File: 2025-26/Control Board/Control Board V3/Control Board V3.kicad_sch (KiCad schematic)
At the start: 0 parts

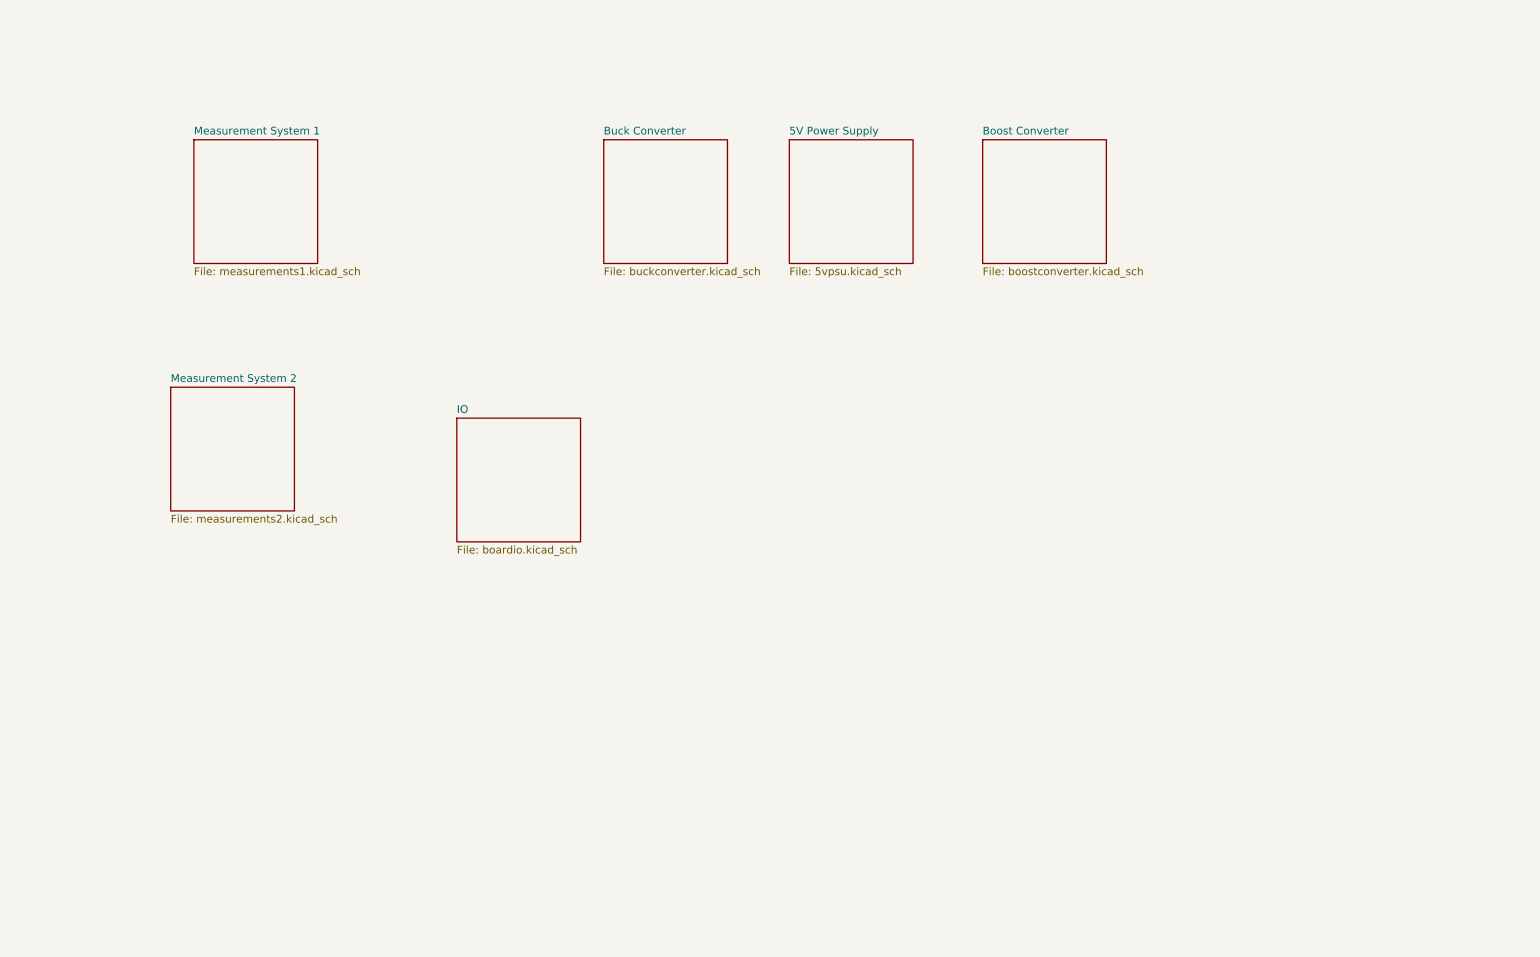
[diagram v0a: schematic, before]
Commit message: board almost fully designed
i want to try a different orientation so gonna push this so i can easily revert
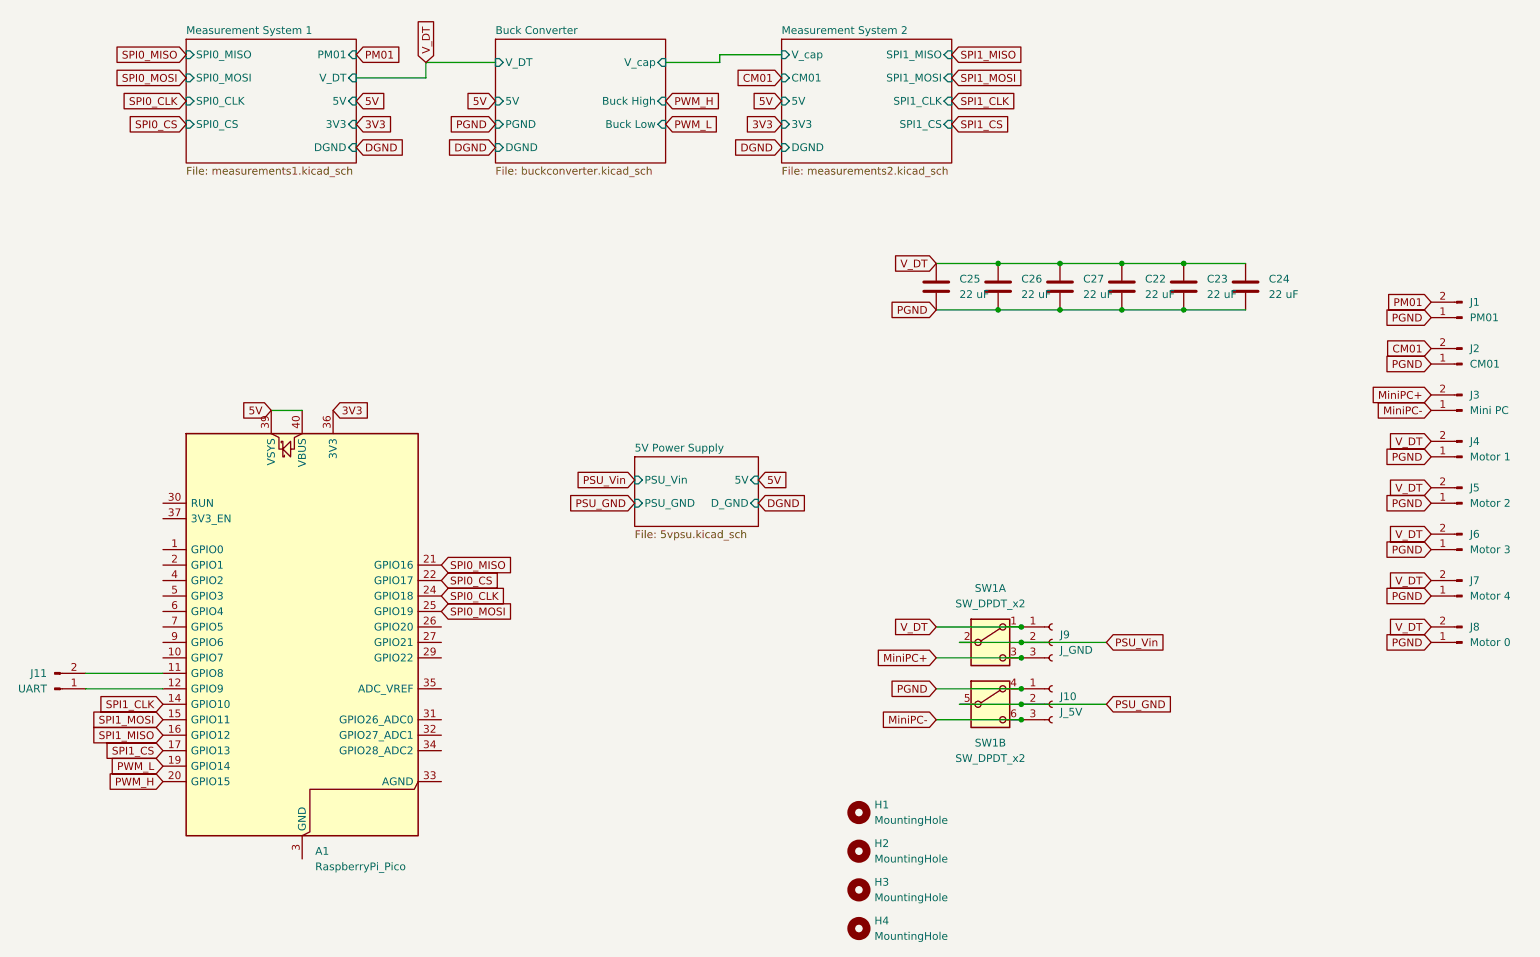
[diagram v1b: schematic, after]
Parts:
- added A1: RaspberryPi_Pico, Module:RaspberryPi_Pico_Common_Unspecified, symbol MCU_Module:RaspberryPi_Pico
- added C22, C23, C24, C25, C26, C27: 22 uF, Capacitor_SMD:C_0805_2012Metric, symbol Device:C
- added H1, H2, H3, H4: MountingHole, MountingHole:MountingHole_3.2mm_M3, symbol Mechanical:MountingHole
- added J1: PM01, Connector_AMASS:AMASS_XT30PW-F_1x02_P2.50mm_Horizontal, symbol Connector:Conn_01x02_Pin
- added J10: J_5V, Connector_PinHeader_2.54mm:PinHeader_1x03_P2.54mm_Vertical, symbol Connector:Conn_01x03_Socket
- added J11: UART, Connector_PinHeader_2.54mm:PinHeader_1x02_P2.54mm_Vertical, symbol Connector:Conn_01x02_Pin
- added J2: CM01, Connector_AMASS:AMASS_XT30PW-F_1x02_P2.50mm_Horizontal, symbol Connector:Conn_01x02_Pin
- added J3: Mini PC, Connector_AMASS:AMASS_XT30PW-F_1x02_P2.50mm_Horizontal, symbol Connector:Conn_01x02_Pin
- added J4: Motor 1, Connector_AMASS:AMASS_XT30PW-F_1x02_P2.50mm_Horizontal, symbol Connector:Conn_01x02_Pin
- added J5: Motor 2, Connector_AMASS:AMASS_XT30PW-F_1x02_P2.50mm_Horizontal, symbol Connector:Conn_01x02_Pin
- added J6: Motor 3, Connector_AMASS:AMASS_XT30PW-F_1x02_P2.50mm_Horizontal, symbol Connector:Conn_01x02_Pin
- added J7: Motor 4, Connector_AMASS:AMASS_XT30PW-F_1x02_P2.50mm_Horizontal, symbol Connector:Conn_01x02_Pin
- added J8: Motor 0, Connector_AMASS:AMASS_XT30PW-F_1x02_P2.50mm_Horizontal, symbol Connector:Conn_01x02_Pin
- added J9: J_GND, Connector_PinHeader_2.54mm:PinHeader_1x03_P2.54mm_Vertical, symbol Connector:Conn_01x03_Socket
- added SW1: SW_DPDT_x2, symbol Switch:SW_DPDT_x2
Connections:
- new net: A1.12 (GPIO9), J11.1 (Pin_1)
- new net: A1.11 (GPIO8), J11.2 (Pin_2)
- new net: A1.13 (GND), A1.18 (GND), A1.23 (GND), A1.28 (GND), A1.3 (GND), A1.38 (GND), A1.8 (GND)
- new net 3V3: A1.36 (3V3)
- new net 5V: A1.39 (VSYS), A1.40 (VBUS)
- new net CM01: J2.2 (Pin_2)
- new net MiniPC+: J3.2 (Pin_2), J9.3 (Pin_3), SW1.3 (C)
- new net MiniPC-: J10.3 (Pin_3), J3.1 (Pin_1), SW1.6 (C)
- new net PGND: C22.2, C23.2, C24.2, C25.2, C26.2, C27.2, J1.1 (Pin_1), J10.1 (Pin_1), J2.1 (Pin_1), J4.1 (Pin_1), J5.1 (Pin_1), J6.1 (Pin_1), J7.1 (Pin_1), J8.1 (Pin_1), SW1.4 (A)
- new net PM01: J1.2 (Pin_2)
- new net PSU_GND: J10.2 (Pin_2), SW1.5 (B)
- new net PSU_Vin: J9.2 (Pin_2), SW1.2 (B)
- new net PWM_H: A1.20 (GPIO15)
- new net PWM_L: A1.19 (GPIO14)
- new net SPI0_CLK: A1.24 (GPIO18)
- new net SPI0_CS: A1.22 (GPIO17)
- new net SPI0_MISO: A1.21 (GPIO16)
- new net SPI0_MOSI: A1.25 (GPIO19)
- new net SPI1_CLK: A1.14 (GPIO10)
- new net SPI1_CS: A1.17 (GPIO13)
- new net SPI1_MISO: A1.16 (GPIO12)
- new net SPI1_MOSI: A1.15 (GPIO11)
- new net V_DT: C22.1, C23.1, C24.1, C25.1, C26.1, C27.1, J4.2 (Pin_2), J5.2 (Pin_2), J6.2 (Pin_2), J7.2 (Pin_2), J8.2 (Pin_2), J9.1 (Pin_1), SW1.1 (A)
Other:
- removed sheet Boost Converter
- removed sheet IO
- sheet 5V Power Supply ports: added 5V, D_GND, PSU_GND, PSU_Vin; removed none
- sheet Buck Converter ports: added 5V, Buck High, Buck Low, DGND, PGND, V_DT, V_cap; removed none
- sheet Measurement System 1 ports: added 3V3, 5V, DGND, PM01, SPI0_CLK, SPI0_CS, SPI0_MISO, SPI0_MOSI, V_DT; removed none
- sheet Measurement System 2 ports: added 3V3, 5V, CM01, DGND, SPI1_CLK, SPI1_CS, SPI1_MISO, SPI1_MOSI, V_cap; removed none
